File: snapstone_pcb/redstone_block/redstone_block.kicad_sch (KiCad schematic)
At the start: 3 parts, among them U2 XIAO-RP2040-NORMAL

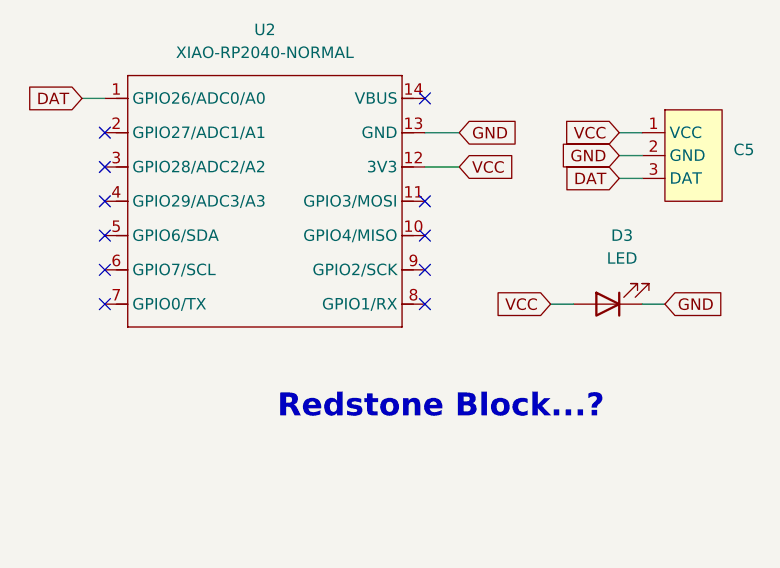
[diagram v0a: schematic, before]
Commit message: Added restone comparator KiCad project
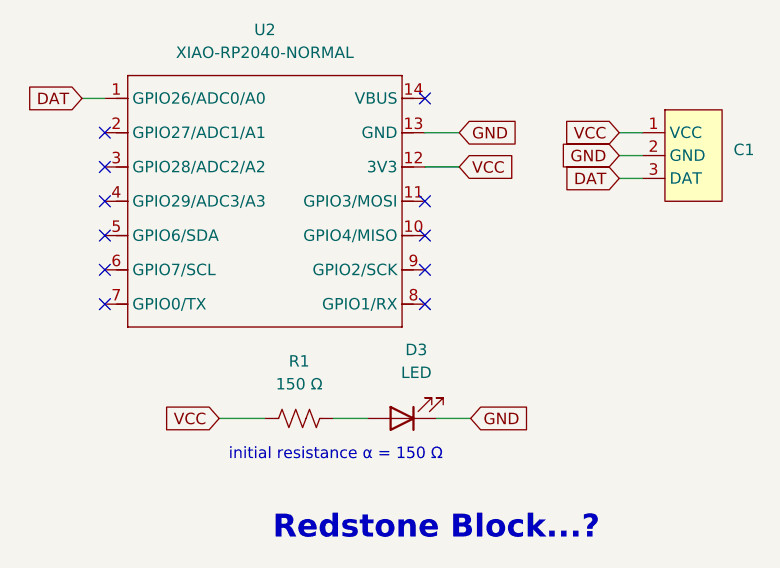
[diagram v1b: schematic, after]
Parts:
- added R1: 150 Ω, symbol Device:R_US
- renumbered C5 to C1
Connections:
- net VCC: now also R1.2; no longer D3.2 (A)
- new net: D3.2 (A), R1.1
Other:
- note added: "initial resistance α = 150 Ω"
- moved on the sheet: D3
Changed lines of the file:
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@@
 	(text "Redstone Block...?\n"
 		(exclude_from_sim no)
-		(at 93.218 81.28 0)
+		(at 92.71 94.742 0)
 		(effects
 			(font
@@
 		)
 	)
+	(text "initial resistance α = 150 Ω"
+		(exclude_from_sim no)
+		(at 81.534 86.614 0)
+		(effects
+			(font
+				(size 1.27 1.27)
+			)
+		)
+	)
 	(no_connect
 		(at 55.88 50.8)
@@
 	(wire
 		(pts
-			(xy 107.95 69.85) (xy 105.41 69.85)
+			(xy 85.09 82.55) (xy 81.28 82.55)
 		)
 		(stroke
@@
 	(wire
 		(pts
+			(xy 73.66 82.55) (xy 68.58 82.55)
+		)
+		(stroke
+			(width 0)
+			(type default)
+		)
+	)
+	(wire
+		(pts
 			(xy 113.03 55.88) (xy 115.57 55.88)
 		)
@@
 	(wire
 		(pts
-			(xy 118.11 69.85) (xy 115.57 69.85)
+			(xy 96.52 82.55) (xy 92.71 82.55)
 		)
 		(stroke
@@
 	(global_label "VCC"
 		(shape input)
-		(at 105.41 69.85 180)
+		(at 68.58 82.55 180)
 		(fields_autoplaced yes)
 		(effects
@@
 		)
 		(property "Intersheetrefs" "${INTERSHEET_REFS}"
-			(at 98.7962 69.85 0)
+			(at 61.9662 82.55 0)
 			(effects
 				(font
@@
 	(global_label "GND"
 		(shape input)
-		(at 118.11 69.85 0)
+		(at 96.52 82.55 0)
 		(fields_autoplaced yes)
 		(effects
@@
 		)
 		(property "Intersheetrefs" "${INTERSHEET_REFS}"
-			(at 124.9657 69.85 0)
+			(at 103.3757 82.55 0)
 			(effects
 				(font
@@
 		(polyline
 			(pts
-				(xy 44.45 36.83) (xy 133.35 36.83) (xy 133.35 76.2) (xy 44.45 76.2)
+				(xy 44.45 36.83) (xy 133.35 36.83) (xy 133.35 90.17) (xy 44.45 90.17)
 			)
 			(stroke
@@
 	)
 	(symbol
-		(lib_id "Device:LED")
-		(at 111.76 69.85 180)
+		(lib_id "Device:R_US")
+		(at 77.47 82.55 270)
 		(unit 1)
 		(exclude_from_sim no)
@@
 		(dnp no)
 		(fields_autoplaced yes)
+		(property "Reference" "R1"
+			(at 77.47 76.2 90)
+			(effects
+				(font
+					(size 1.27 1.27)
+				)
+			)
+		)
+		(property "Value" "150 Ω"
+			(at 77.47 78.74 90)
+			(effects
+				(font
+					(size 1.27 1.27)
+				)
+			)
+		)
+		(property "Footprint" ""
+			(at 77.216 83.566 90)
+			(effects
+				(font
+					(size 1.27 1.27)
+				)
+				(hide yes)
+			)
+		)
+		(property "Datasheet" "~"
+			(at 77.47 82.55 0)
+			(effects
+				(font
+					(size 1.27 1.27)
+				)
+				(hide yes)
+			)
+		)
+		(property "Description" "Resistor, US symbol"
+			(at 77.47 82.55 0)
+			(effects
+				(font
+					(size 1.27 1.27)
+				)
+				(hide yes)
+			)
+		)
+		(pin "2"
+		)
+		(pin "1"
+		)
+		(instances
+			(project ""
+				(path "/a21feee3-f94a-4c16-9306-59a893425ad2"
+					(reference "R1")
+					(unit 1)
+				)
+			)
+		)
+	)
+	(symbol
+		(lib_id "Device:LED")
+		(at 88.9 82.55 180)
+		(unit 1)
+		(exclude_from_sim no)
+		(in_bom yes)
+		(on_board yes)
+		(dnp no)
+		(fields_autoplaced yes)
 		(property "Reference" "D3"
-			(at 113.3475 62.23 0)
+			(at 90.4875 74.93 0)
 			(effects
 				(font
@@
 		)
 		(property "Value" "LED"
-			(at 113.3475 64.77 0)
+			(at 90.4875 77.47 0)
 			(effects
 				(font
@@
 		)
 		(property "Footprint" ""
-			(at 111.76 69.85 0)
+			(at 88.9 82.55 0)
 			(effects
 				(font
@@
 		)
 		(property "Datasheet" "~"
-			(at 111.76 69.85 0)
+			(at 88.9 82.55 0)
 			(effects
 				(font
@@
 		)
 		(property "Description" "Light emitting diode"
-			(at 111.76 69.85 0)
+			(at 88.9 82.55 0)
 			(effects
 				(font
@@
 		)
 		(property "Sim.Pins" "1=K 2=A"
-			(at 111.76 69.85 0)
+			(at 88.9 82.55 0)
 			(effects
 				(font
@@
 		(dnp no)
 		(fields_autoplaced yes)
-		(property "Reference" "C5"
+		(property "Reference" "C1"
 			(at 125.73 52.7049 0)
 			(effects
@@
 			(project "redstone_block"
 				(path "/a21feee3-f94a-4c16-9306-59a893425ad2"
-					(reference "C5")
+					(reference "C1")
 					(unit 1)
 				)

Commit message: Added redstone comparator project!
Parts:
- removed U2: XIAO-RP2040-NORMAL, Module:MOUDLE14P-XIAO-DIP-SMD, symbol Seeed_Studio_XIAO_Series:XIAO-RP2040-NORMAL
- added D1, D2, D4, D5: LED, symbol Device:LED
- renumbered C1 to C_OUT1
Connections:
- net GND: no longer D3.1 (K)
- net at D3.2 (A), R1.1: now also D1.2 (A), D2.2 (A), D4.2 (A), D5.2 (A)
- net DAT: no longer names the net of C_OUT1.3 (DAT)
- net DAT: now also D3.1 (K), D1.1 (K), D2.1 (K), D4.1 (K), D5.1 (K)
- no-connect marks 11 -> 0
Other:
- note added: "Lighting & Resistor"
- note removed: "Redstone Block...?"
- moved on the sheet: C_OUT1, R1

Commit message: oops, forgot the redstone_block/ files 🥀😭🙏
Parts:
- removed D1, D2, D3, D4, D5: LED, symbol Device:LED
- added BT1: 2468_Battery_Holder, 2468_Battery_Holder:BAT_2468, symbol 2468_Battery_Holder:2468
- added C_OUT_LED1, C_OUT_LED2: ~, 691137710003_Board_To_Wire:691137710003_Board_To_Wire, symbol snapstone:3_Pin_Block_Connector
- C_OUT1: footprint (none) -> 691137710003_Board_To_Wire:691137710003_Board_To_Wire
- R1: footprint (none) -> CF12JT150R_Resistor_150:STA_CF12_STP
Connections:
- net GND: now also BT1.N
- net VCC: now also BT1.P
- net at C_OUT1.3 (DAT): now also R1.1, C_OUT_LED1.3 (DAT), C_OUT_LED2.3 (DAT)
- no-connect marks 0 -> 4
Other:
- note added: "Battery & Power"
- note added: "Use 2 AAA batteries, 1.5 V each. The 2-battery holder wires them in series, outputting 3V."
- moved on the sheet: C_OUT1, R1

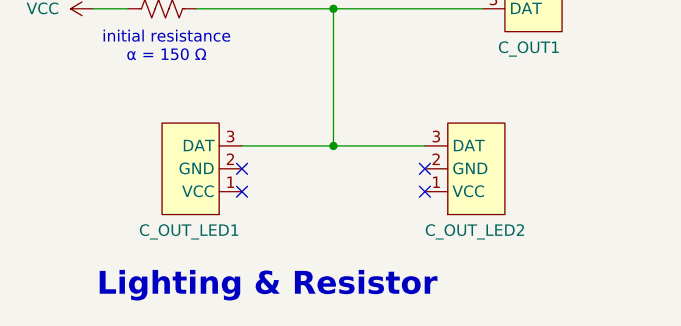
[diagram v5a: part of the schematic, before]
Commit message: Updated resistor footprint project-wide
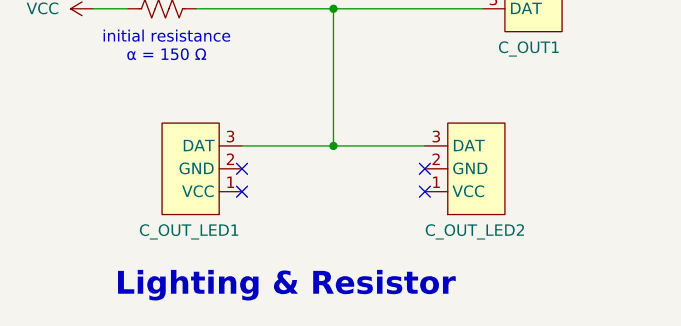
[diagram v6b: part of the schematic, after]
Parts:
- C_OUT1, C_OUT_LED1, C_OUT_LED2: value ~ -> (none)
- R1: footprint CF12JT150R_Resistor_150:STA_CF12_STP -> CF12JT_Resistor:STA_CF12_STP

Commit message: Made PCB for observer & redstone block!
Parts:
- added C_OUT2, C_OUT3, C_OUT4: (no value), 691137710003_Board_To_Wire:691137710003_Board_To_Wire, symbol snapstone:3_Pin_Block_Connector
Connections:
- net GND: now also C_OUT_LED1.2 (GND), C_OUT_LED2.2 (GND), C_OUT2.2 (GND), C_OUT3.2 (GND), C_OUT4.2 (GND)
- net VCC: now also C_OUT2.1 (VCC), C_OUT3.1 (VCC), C_OUT4.1 (VCC)
- net OUT: now reaches C_OUT1.3 (DAT), C_OUT_LED1.3 (DAT), C_OUT_LED2.3 (DAT), R1.1
- net OUT: now also C_OUT2.3 (DAT), C_OUT3.3 (DAT), C_OUT4.3 (DAT)
- no-connect marks 4 -> 2
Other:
- note added: "Outputs (All Sides)"
- moved on the sheet: BT1, C_OUT_LED1, C_OUT_LED2, R1
